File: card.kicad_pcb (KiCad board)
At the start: 2 copper layers, 88.8 x 50.7 mm, 25 parts, among them J1 Conn_02x03_Odd_Even, P2_FPC24/0.5MM1 Conn_01x24_Male, Q1 Si1308EDL, U1 ATMEGA168PA-AU

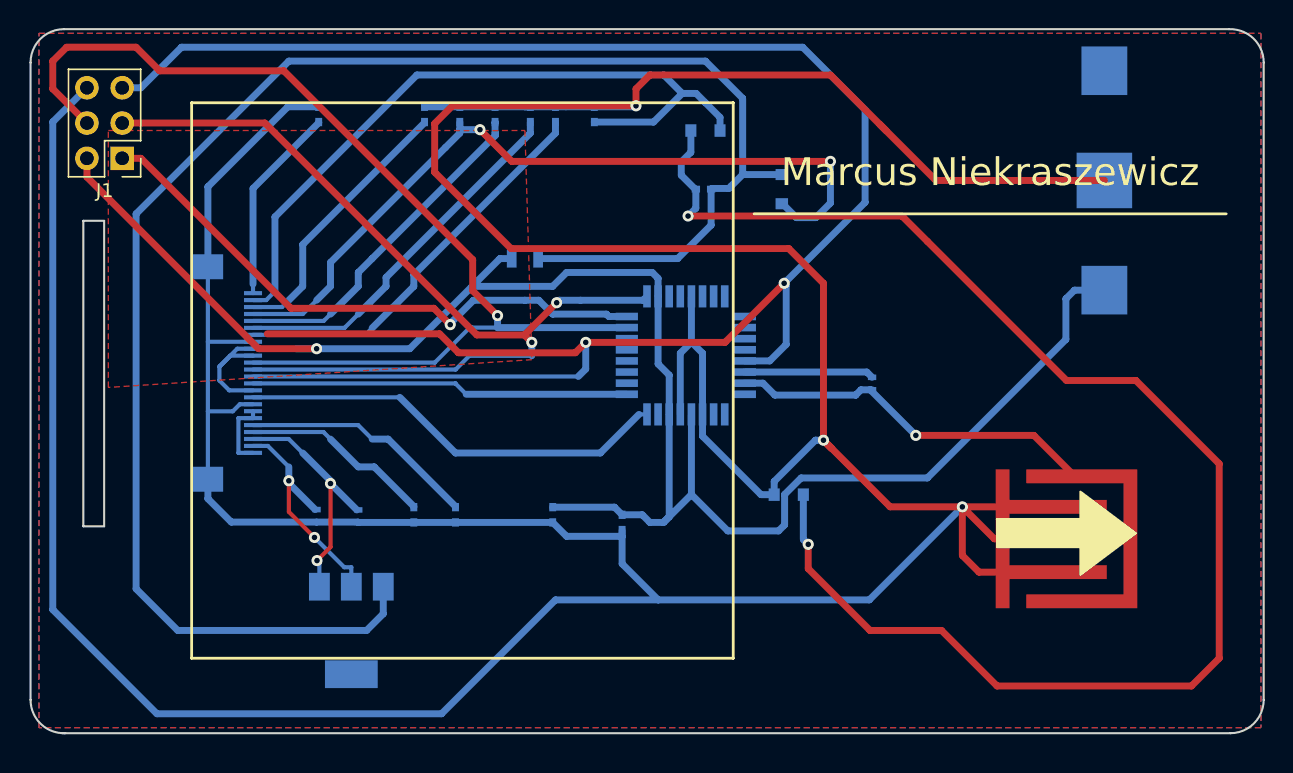
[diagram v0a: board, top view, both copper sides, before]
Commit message: fixed FPC connector footprint, updated traces
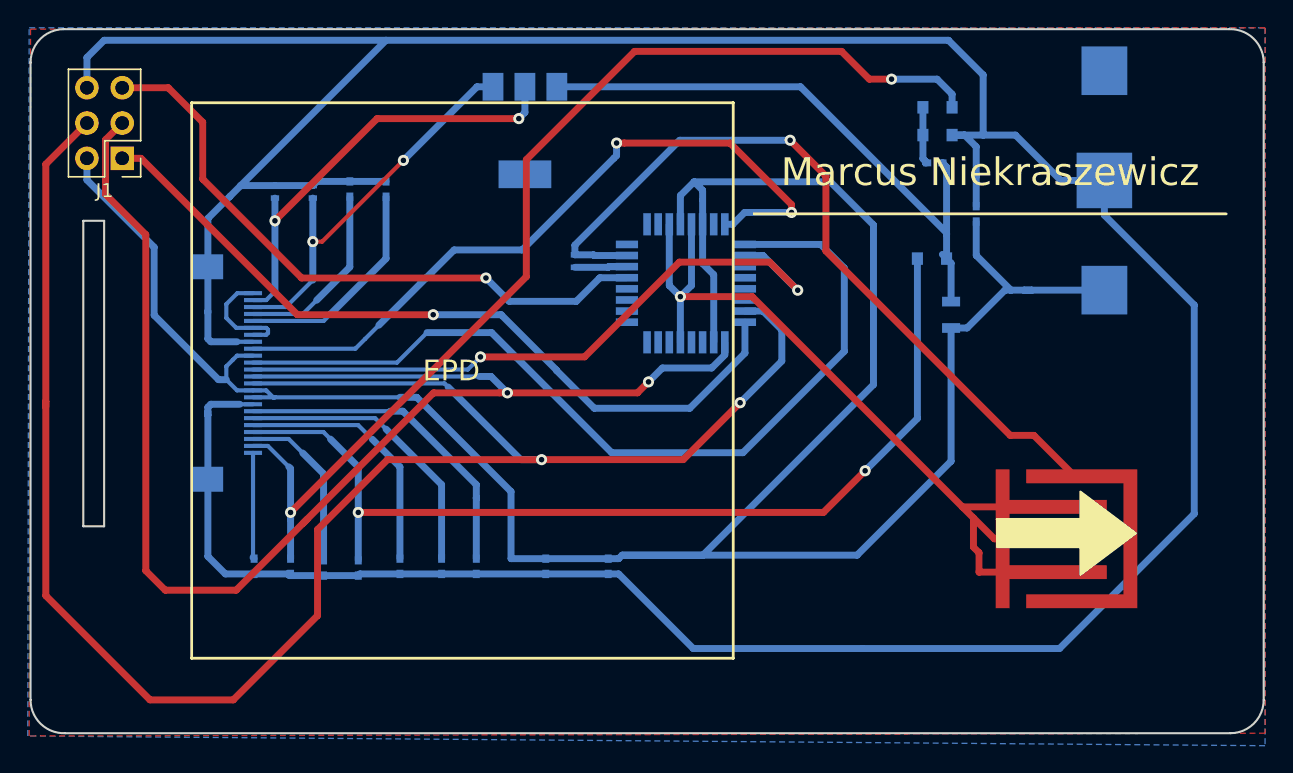
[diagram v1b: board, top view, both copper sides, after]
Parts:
- removed ?: C, Buttons_Switches_SMD:Touchpad
- added  : C, Buttons_Switches_SMD:Touchpad, F.Cu at (175.0, 132.0)
- added C1: 4.7uf1, Capacitors_SMD:C_0402, B.Cu at (142.0, 126.4)
- P2_FPC24/0.5MM1: footprint Connectors_FPC:Hirose_FH12-24S-0.5SH_1x24_P0.50mm_Horizontal_Gnd17 -> Connectors_FPC:Hirose_FH12-24S-0.5SH_1x24_P0.50mm_Horizontal_Gnd17_Mirr
- moved 1uF2 39.2 mm to (119.1, 126.4), turned to 270 degrees
- moved Q1 38.1 mm to (136.0, 95.0)
- moved 4.7uf1 37.4 mm to (168.5, 101.0), turned to 270 degrees
- moved 1uF4 33.5 mm to (124.0, 126.5), turned to 270 degrees
- moved 1uF3 33.5 mm to (121.5, 126.5), turned to 270 degrees
- moved 1uF5 33.3 mm to (127.0, 126.4), turned to 270 degrees
- moved 1uF6 33.2 mm to (130.0, 126.4), turned to 270 degrees
- moved 1uF7 33.0 mm to (132.5, 126.4), turned to 270 degrees
- moved 1uF1 32.9 mm to (116.5, 126.4), turned to 270 degrees
- moved 10uH1 31.0 mm to (166.7, 108.3), turned to 90 degrees
- moved D1 28.0 mm to (165.7, 95.3), turned to 180 degrees
- moved 1uF8 24.0 mm to (126.0, 99.2), turned to 90 degrees
- moved 1uF9 23.9 mm to (123.4, 99.2), turned to 90 degrees
- moved R3 23.6 mm to (120.7, 99.4), turned to 90 degrees
- moved R10k1 23.5 mm to (118.0, 99.4), turned to 270 degrees
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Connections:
- P2_FPC24/0.5MM1 pad 12: Net-(J1-Pad5) -> Net-(P2_FPC24/0.5MM1-Pad12)
- U1 pad 10: Net-(U1-Pad10) -> Net-(P2_FPC24/0.5MM1-Pad12)
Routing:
- net Net-(4.7uf2-Pad2): track 106.2 -> 4.30 mm, vias 2 -> 0
- net Net-(J1-Pad5): track 145.4 -> 45.8 mm, vias 2 -> 1
- net Net-(10uH1-Pad2): track 124.9 -> 43.6 mm
- net Net-(J1-Pad4): track 76.7 -> 134.2 mm, vias 1 -> 2
- net GND: track 369.8 -> 313.4 mm, vias 3 -> 1
- net Net-(P2_FPC24/0.5MM1-Pad12): track 0.00 -> 48.1 mm, vias 0 -> 2
- net Net-(P2_FPC24/0.5MM1-Pad11): track 27.3 -> 65.1 mm
- net Net-(0.01uF1-Pad1): track 143.8 -> 181.3 mm, vias 1 -> 0
- net Net-(J1-Pad3): track 67.5 -> 103.6 mm
- net Net-(Ctouch1-Pad1): track 46.6 -> 77.8 mm
- net Net-(1uF2-Pad1): track 52.9 -> 78.9 mm, vias 0 -> 2
- net Net-(P2_FPC24/0.5MM1-Pad9): track 31.2 -> 53.0 mm, vias 0 -> 2
- net Net-(P2_FPC24/0.5MM1-Pad2): track 17.0 -> 31.6 mm
- net Net-(J1-Pad1): track 42.6 -> 56.2 mm
- net Net-(1uF4-Pad1): track 57.1 -> 69.9 mm
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- removed copper zone on F.Cu, net Net-(J1-Pad1)
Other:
- outline, holes or cut-outs redrawn
- board text added: "EPD"

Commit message: increased some footprint sizes, added missing via
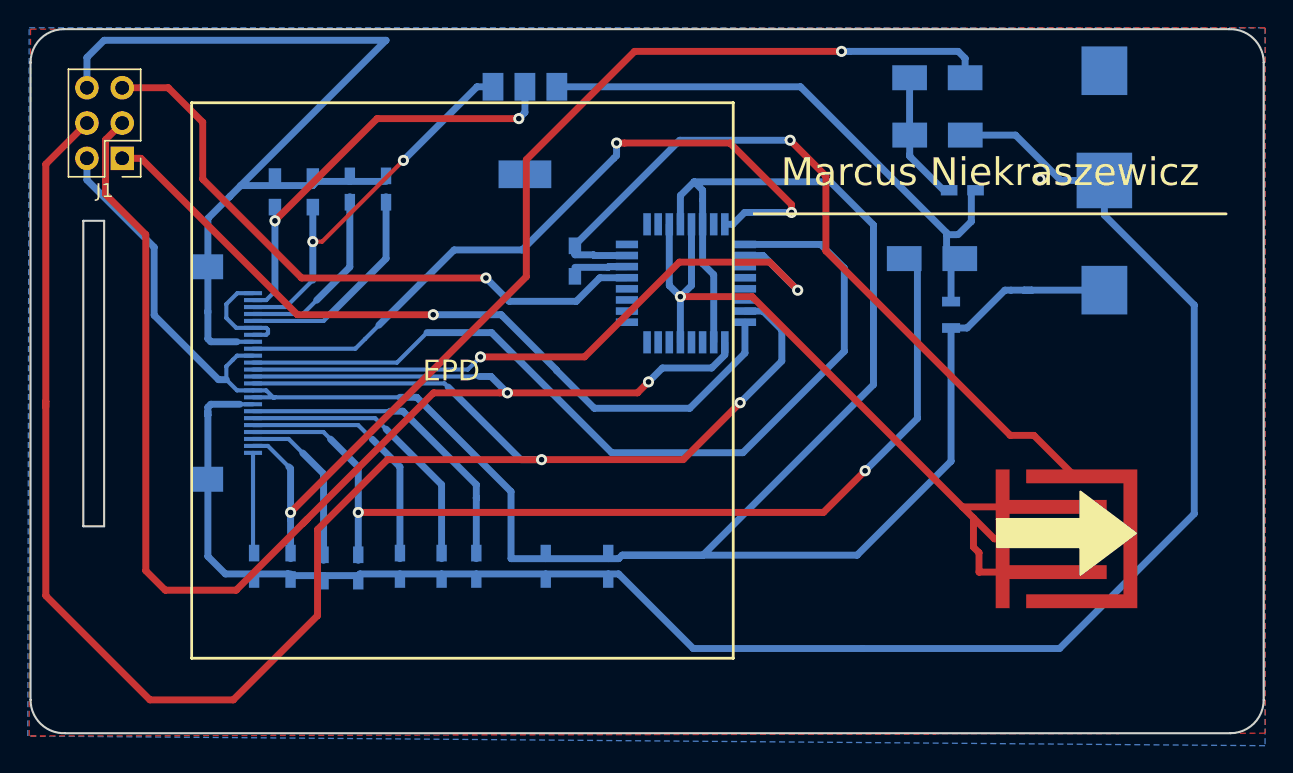
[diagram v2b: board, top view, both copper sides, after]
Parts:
- removed 4.7uf1: C, Capacitors_SMD:C_0402
- 0.01uF1, 1uF1, 1uF2, 1uF3, 1uF4, 1uF5, 1uF6, 1uF7, 1uF8, 1uF9, 4.7uf2, C1: footprint Capacitors_SMD:C_0402 -> Capacitors_SMD:C_0603_HandSoldering
- D1, D2, D3: footprint Diodes_SMD:D_0805 -> Diodes_SMD:D_SMA
- R10k1, R3, Rtouch1: footprint Resistors_SMD:R_0402 -> Resistors_SMD:R_0603_HandSoldering
- moved 4.7uf2 2.80 mm to (167.5, 99.3)
- moved D2 2.13 mm to (165.7, 91.2)
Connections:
- U1 pad 11: Net-(U1-Pad11) -> Net-(P2_FPC24/0.5MM1-Pad9)
- U1 pad 8: Net-(P2_FPC24/0.5MM1-Pad9) -> Net-(U1-Pad8)
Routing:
- net GND: track 313.4 -> 259.5 mm, vias 1 -> 2
- net Net-(0.01uF1-Pad1): track 181.3 -> 175.3 mm
- net Net-(4.7uf2-Pad2): track 4.30 -> 9.11 mm
- net Net-(10uH1-Pad2): track 43.6 -> 42.3 mm
- net Net-(P2_FPC24/0.5MM1-Pad3): track 28.6 -> 28.0 mm
- net Net-(P2_FPC24/0.5MM1-Pad2): track 31.6 -> 31.0 mm
- net Net-(U1-Pad8): track 0.00 -> 0.58 mm
- net Net-(P2_FPC24/0.5MM1-Pad9): track 53.0 -> 52.4 mm

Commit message: Connected display reset to AVR, increased inductor footprint size.
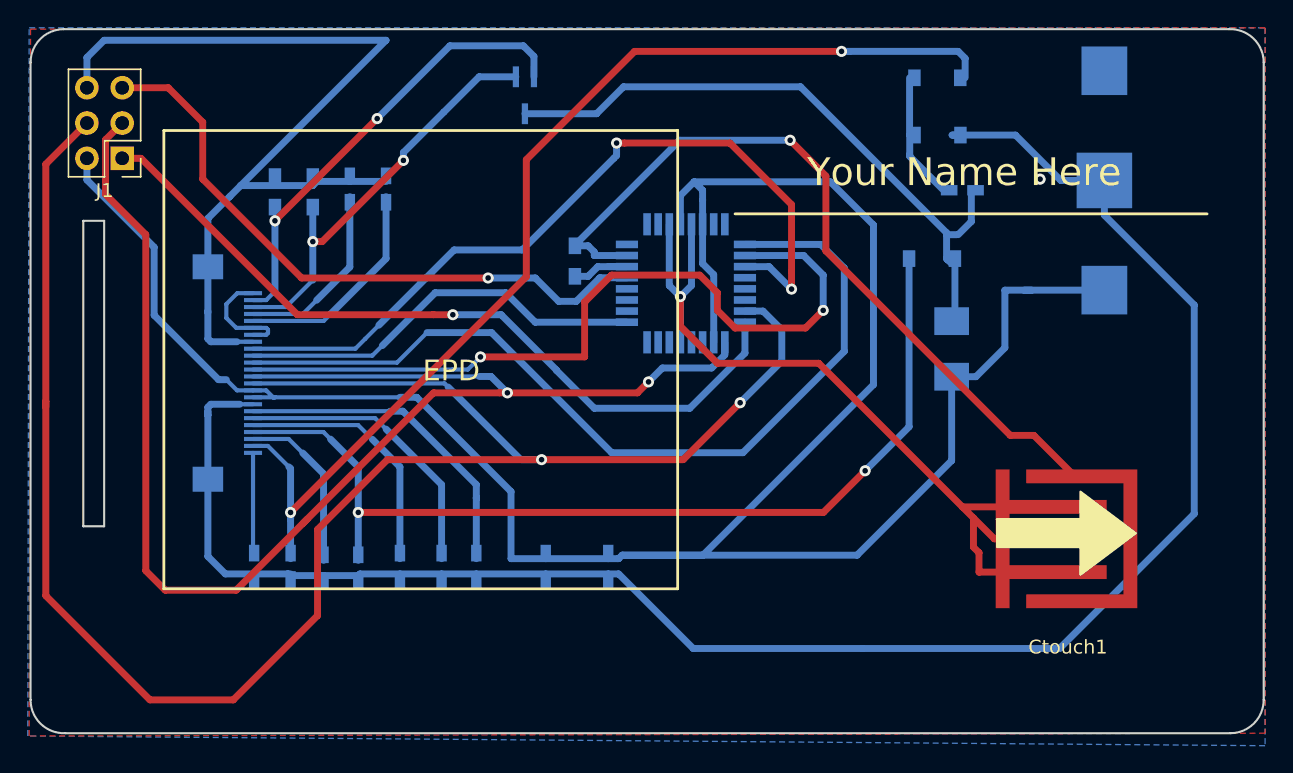
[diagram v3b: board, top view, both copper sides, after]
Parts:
- 10uH1: footprint Inductors_SMD:L_0805 -> Inductors_SMD:L_1210_HandSoldering
- Ctouch1: renamed from  
- D1, D2, D3: footprint Diodes_SMD:D_SMA -> Diodes_SMD:D_SOD-123
- Q1: footprint TO_SOT_Packages_SMD:SOT-223 -> TO_SOT_Packages_SMD:SOT-323_SC-70_Handsoldering
- Rtouch1: value R -> 1M
- moved Q1 2.54 mm to (136.0, 92.5)
- moved 10uH1 2.46 mm to (166.7, 110.7)
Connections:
- net Net-(1uF2-Pad1) renamed /PREVGL
- net Net-(1uF4-Pad1) renamed /PREVGH
- net Net-(J1-Pad3) renamed /SCLK
- net Net-(J1-Pad4) renamed /SDI
- net Net-(P2_FPC24/0.5MM1-Pad11) renamed /DC
- net Net-(P2_FPC24/0.5MM1-Pad12) renamed /CS
- net Net-(P2_FPC24/0.5MM1-Pad2) renamed /GDR
- net Net-(P2_FPC24/0.5MM1-Pad3) renamed /RESE
- net Net-(P2_FPC24/0.5MM1-Pad9) renamed /BUSY
- P2_FPC24/0.5MM1 pad 10: Net-(0.01uF1-Pad1) -> /RES
- U1 pad 25: Net-(U1-Pad25) -> /RES
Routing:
- net /RES: track 0.00 -> 29.7 mm
- net /CS: track 48.1 -> 57.8 mm
- net Net-(10uH1-Pad2): track 42.3 -> 47.6 mm
- net /BUSY: track 52.4 -> 57.4 mm
- net Net-(0.01uF1-Pad1): track 175.3 -> 172.6 mm
- net /GDR: track 31.0 -> 33.6 mm
- net /RESE: track 28.0 -> 30.2 mm
- net GND: track 259.5 -> 260.8 mm
- net Net-(U1-Pad8): track 0.58 -> 0.00 mm
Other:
- board text added: "Your Name Here"
- board text removed: "Marcus Niekraszewicz"
